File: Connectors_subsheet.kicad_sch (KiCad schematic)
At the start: 29 parts, among them J10 IMU_1, J11 USB_A, J12 Power_Connector, J3 Ultrasonic, J9 IMU_2, Q1 BSS138

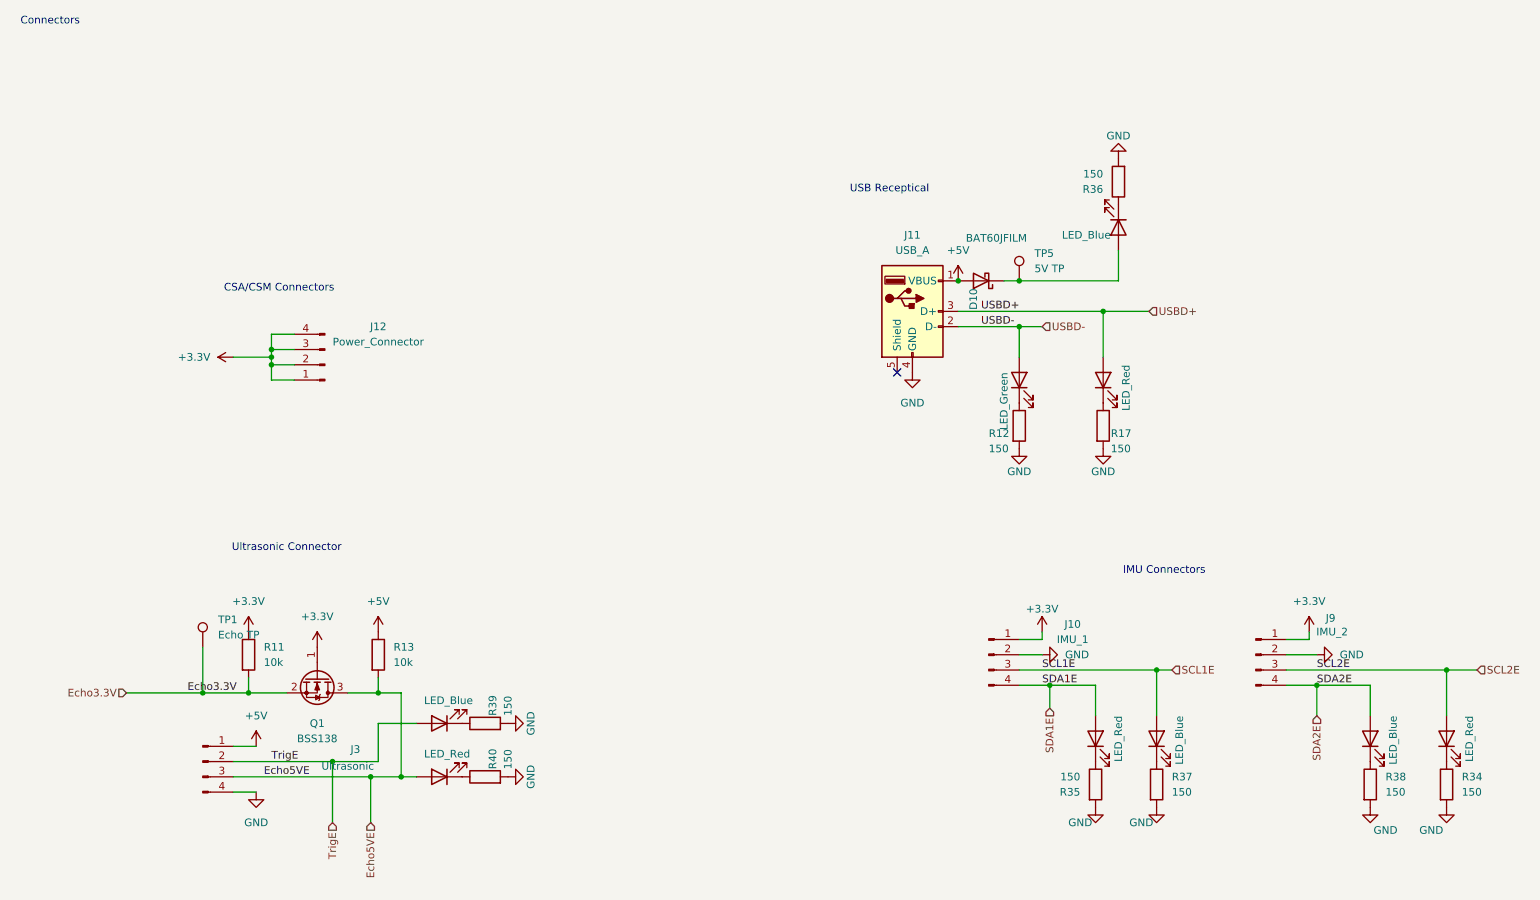
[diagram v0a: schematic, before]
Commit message: remove un-needed program header circuitry, add debug LEDs, add USB ESD, add shcotty for LM117
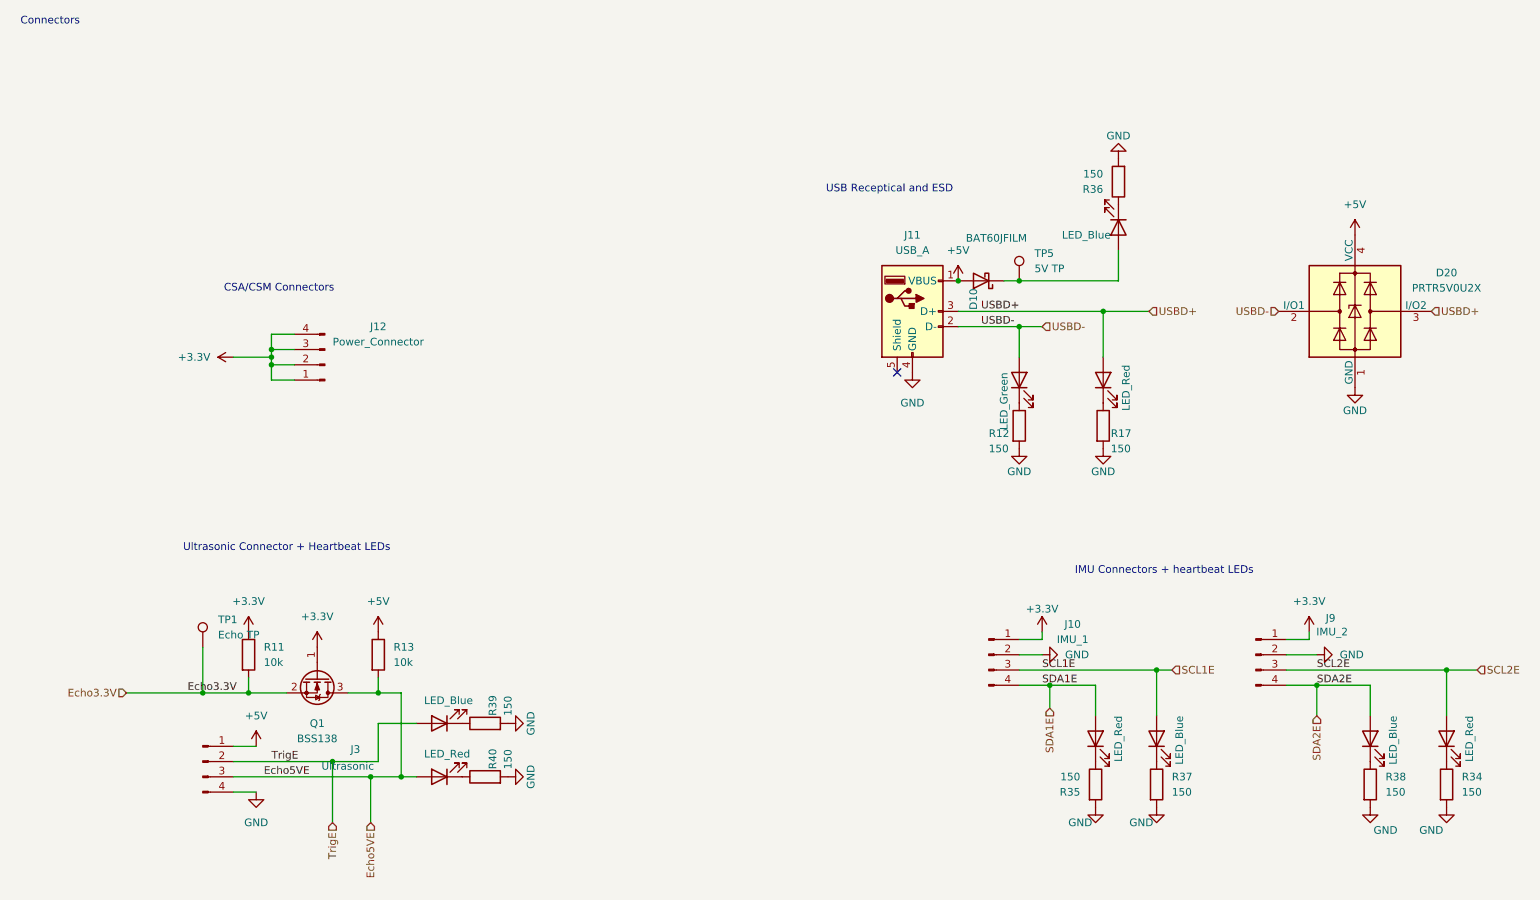
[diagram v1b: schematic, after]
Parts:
- added D20: PRTR5V0U2X, Package_TO_SOT_SMD:SOT-143, symbol Power_Protection:PRTR5V0U2X
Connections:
- net +5V: now also D20.4 (VCC)
- net GND: now also D20.1 (GND)
- net USBD+: now also D20.3 (I/O2)
- net USBD-: now also D20.2 (I/O1)
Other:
- note added: "IMU Connectors + heartbeat LEDs"
- note added: "USB Receptical and ESD"
- note added: "Ultrasonic Connector + Heartbeat LEDs"
- note removed: "IMU Connectors"
- note removed: "USB Receptical"
- note removed: "Ultrasonic Connector"
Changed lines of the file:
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@@
 		)
 	)
-	(text "Ultrasonic Connector"
+	(text "Ultrasonic Connector + Heartbeat LEDs"
 		(exclude_from_sim no)
 		(at 68.58 110.49 0)
@@
 		)
 	)
-	(text "USB Receptical\n"
+	(text "USB Receptical and ESD\n"
 		(exclude_from_sim no)
 		(at 168.91 50.8 0)
@@
 		)
 	)
-	(text "IMU Connectors\n"
+	(text "IMU Connectors + heartbeat LEDs\n"
 		(exclude_from_sim no)
 		(at 214.63 114.3 0)
@@
 		)
 	)
+	(hierarchical_label "USBD+"
+		(shape input)
+		(at 259.08 71.12 0)
+		(fields_autoplaced yes)
+		(effects
+			(font
+				(size 1.27 1.27)
+			)
+			(justify left)
+		)
+	)
 	(hierarchical_label "SDA1E"
 		(shape input)
@@
 		)
 	)
+	(hierarchical_label "USBD-"
+		(shape input)
+		(at 233.68 71.12 180)
+		(fields_autoplaced yes)
+		(effects
+			(font
+				(size 1.27 1.27)
+			)
+			(justify right)
+		)
+	)
 	(symbol
 		(lib_id "power:GND")
@@
 	)
 	(symbol
+		(lib_id "power:GND")
+		(at 246.38 83.82 0)
+		(unit 1)
+		(exclude_from_sim no)
+		(in_bom yes)
+		(on_board yes)
+		(dnp no)
+		(property "Reference" "#PWR033"
+			(at 246.38 90.17 0)
+			(effects
+				(font
+					(size 1.27 1.27)
+				)
+				(hide yes)
+			)
+		)
+		(property "Value" "GND"
+			(at 246.38 87.63 0)
+			(effects
+				(font
+					(size 1.27 1.27)
+				)
+			)
+		)
+		(property "Footprint" ""
+			(at 246.38 83.82 0)
+			(effects
+				(font
+					(size 1.27 1.27)
+				)
+				(hide yes)
+			)
+		)
+		(property "Datasheet" ""
+			(at 246.38 83.82 0)
+			(effects
+				(font
+					(size 1.27 1.27)
+				)
+				(hide yes)
+			)
+		)
+		(property "Description" "Power symbol creates a global label with name \"GND\" , ground"
+			(at 246.38 83.82 0)
+			(effects
+				(font
+					(size 1.27 1.27)
+				)
+				(hide yes)
+			)
+		)
+		(pin "1"
+		)
+		(instances
+			(project "PCB_Schematic"
+				(path "/a0c17764-e0d1-4df5-b871-1489cf266494/ca0ff4d7-ae36-445b-939c-5f82f56efbb4"
+					(reference "#PWR033")
+					(unit 1)
+				)
+			)
+		)
+	)
+	(symbol
 		(lib_id "Device:R")
 		(at 101.6 139.7 90)
@@
 	(symbol
 		(lib_id "power:+5V")
+		(at 246.38 58.42 0)
+		(unit 1)
+		(exclude_from_sim no)
+		(in_bom yes)
+		(on_board yes)
+		(dnp no)
+		(fields_autoplaced yes)
+		(property "Reference" "#PWR038"
+			(at 246.38 62.23 0)
+			(effects
+				(font
+					(size 1.27 1.27)
+				)
+				(hide yes)
+			)
+		)
+		(property "Value" "+5V"
+			(at 246.38 53.34 0)
+			(effects
+				(font
+					(size 1.27 1.27)
+				)
+			)
+		)
+		(property "Footprint" ""
+			(at 246.38 58.42 0)
+			(effects
+				(font
+					(size 1.27 1.27)
+				)
+				(hide yes)
+			)
+		)
+		(property "Datasheet" ""
+			(at 246.38 58.42 0)
+			(effects
+				(font
+					(size 1.27 1.27)
+				)
+				(hide yes)
+			)
+		)
+		(property "Description" "Power symbol creates a global label with name \"+5V\""
+			(at 246.38 58.42 0)
+			(effects
+				(font
+					(size 1.27 1.27)
+				)
+				(hide yes)
+			)
+		)
+		(pin "1"
+		)
+		(instances
+			(project "PCB_Schematic"
+				(path "/a0c17764-e0d1-4df5-b871-1489cf266494/ca0ff4d7-ae36-445b-939c-5f82f56efbb4"
+					(reference "#PWR038")
+					(unit 1)
+				)
+			)
+		)
+	)
+	(symbol
+		(lib_id "power:+5V")
 		(at 83.82 124.46 0)
 		(unit 1)
@@
 					(unit 1)
 				)
+			)
+		)
+	)
+	(symbol
+		(lib_id "Power_Protection:PRTR5V0U2X")
+		(at 246.38 71.12 0)
+		(unit 1)
+		(exclude_from_sim no)
+		(in_bom yes)
+		(on_board yes)
+		(dnp no)
+		(fields_autoplaced yes)
+		(property "Reference" "D20"
+			(at 261.62 64.6998 0)
+			(effects
+				(font
+					(size 1.27 1.27)
+				)
+			)
+		)
+		(property "Value" "PRTR5V0U2X"
+			(at 261.62 67.2398 0)
+			(effects
+				(font
+					(size 1.27 1.27)
+				)
+			)
+		)
+		(property "Footprint" "Package_TO_SOT_SMD:SOT-143"
+			(at 247.904 71.12 0)
+			(effects
+				(font
+					(size 1.27 1.27)
+				)
+				(hide yes)
+			)
+		)
+		(property "Datasheet" "https://assets.nexperia.com/documents/data-sheet/PRTR5V0U2X.pdf"
+			(at 247.904 71.12 0)
+			(effects
+				(font
+					(size 1.27 1.27)
+				)
+				(hide yes)
+			)
+		)
+		(property "Description" "Ultra low capacitance double rail-to-rail ESD protection diode, SOT-143"
+			(at 246.38 71.12 0)
+			(effects
+				(font
+					(size 1.27 1.27)
+				)
+				(hide yes)
+			)
+		)
+		(pin "1"
+		)
+		(pin "3"
+		)
+		(pin "4"
+		)
+		(pin "2"
+		)
+		(instances
+			(project ""
+				(path "/a0c17764-e0d1-4df5-b871-1489cf266494/ca0ff4d7-ae36-445b-939c-5f82f56efbb4"
+					(reference "D20")
+					(unit 1)
+				)

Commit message: starter PCB
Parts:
- renumbered D33 to D14, D34 to D15, D10 to D16, D9 to D17, D31 to D18, D13 to D19, D32 to D20, D35 to D21, D20 to D22, D36 to D23, D14 to D24, J12 to J4, J11 to J5, J10 to J6, J9 to J7, R11 to R16, R13 to R17, R39 to R18, R40 to R19, R12 to R20, R35 to R21, R17 to R22, R36 to R23, R37 to R24, R38 to R25, R34 to R26, TP1 to TP2, TP5 to TP3

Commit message: routing v1
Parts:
- added J8: SDOAG_Connector, Library:CONN_B4B-XH-A_JSTProject, symbol Connector:Conn_01x04_Pin
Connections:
- net GND: now also J8.1 (Pin_1), J8.2 (Pin_2), J8.3 (Pin_3), J8.4 (Pin_4)
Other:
- note added: "SDOAG Connectors"
- moved on the sheet: J4

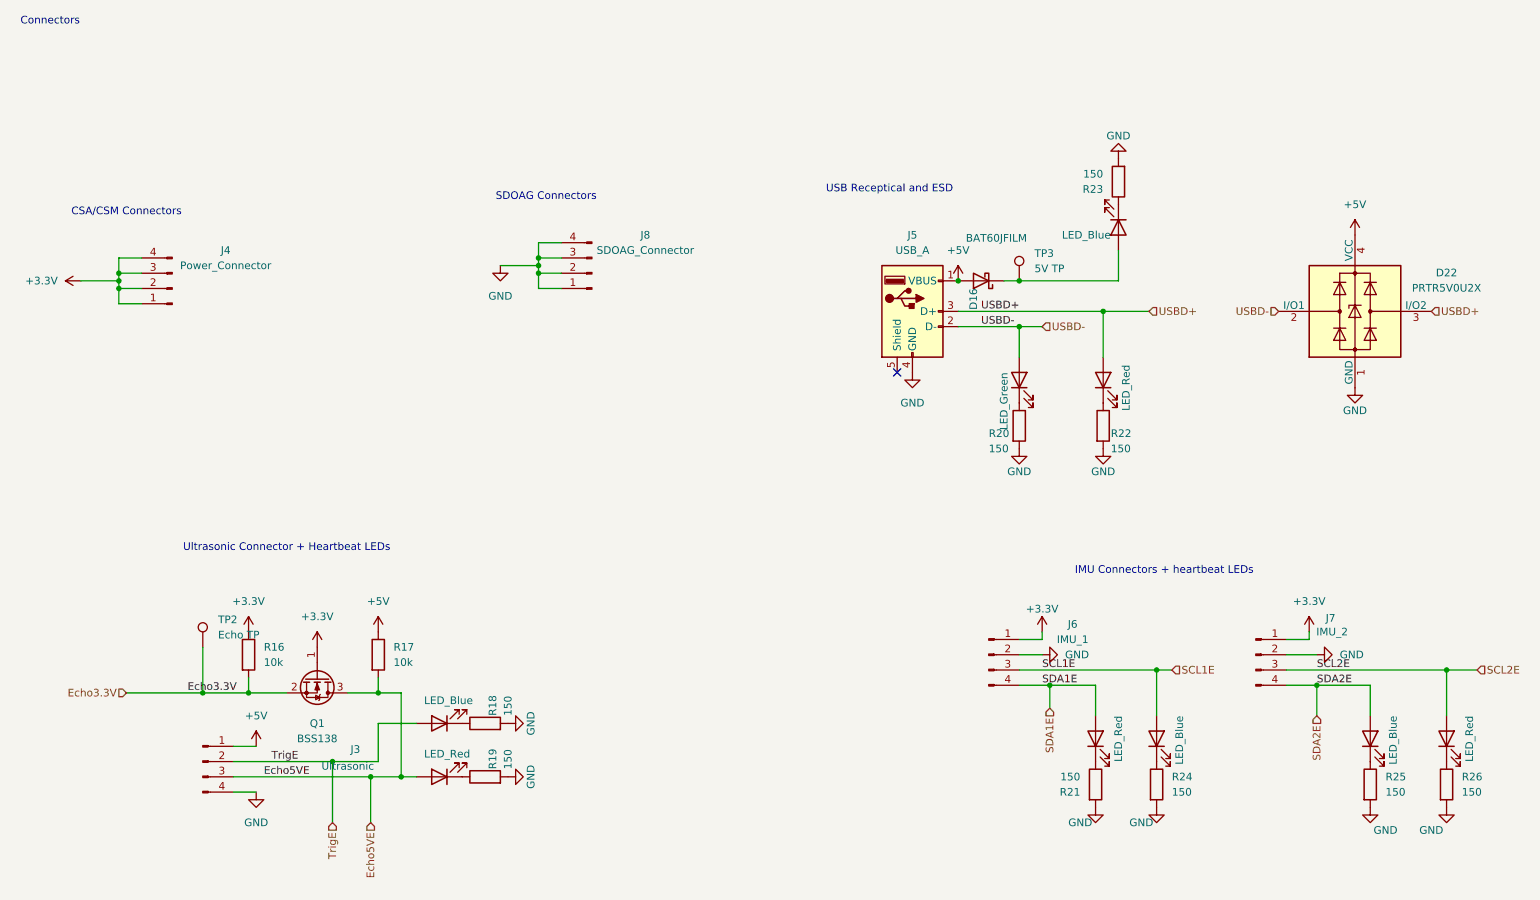
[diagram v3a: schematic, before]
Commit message: added testpoints to schematic for important sigs
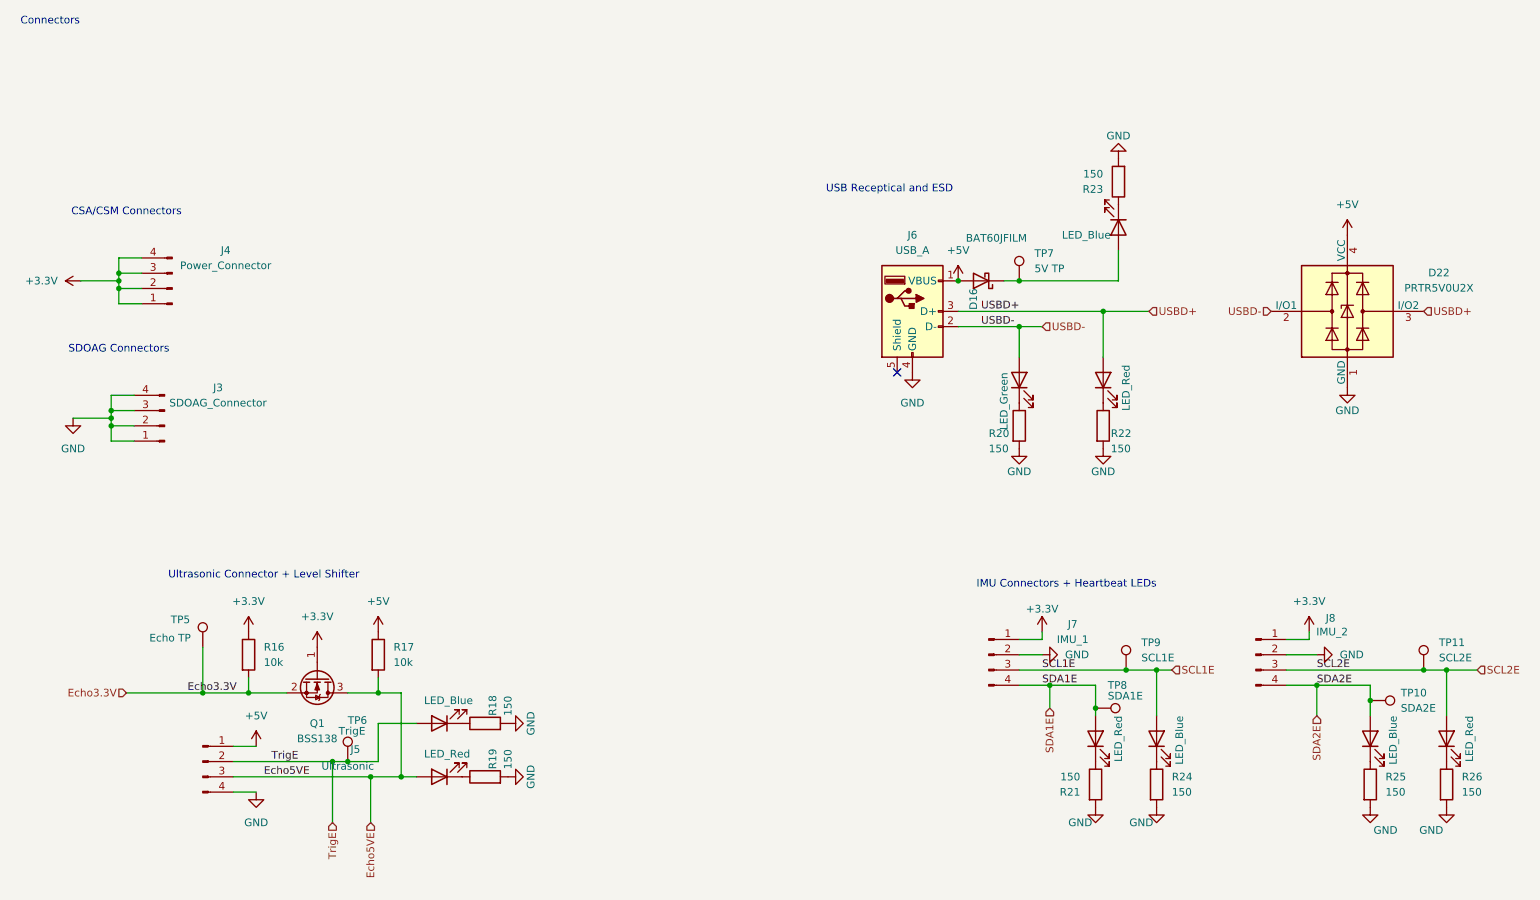
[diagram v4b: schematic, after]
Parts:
- added TP10: SDA2E, symbol Connector:TestPoint
- added TP11: SCL2E, symbol Connector:TestPoint
- added TP6: TrigE, symbol Connector:TestPoint
- added TP8: SDA1E, symbol Connector:TestPoint
- added TP9: SCL1E, symbol Connector:TestPoint
- renumbered J8 to J3, J3 to J5, J5 to J6, J6 to J7, J7 to J8, TP2 to TP5, TP3 to TP7
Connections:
- net SCL1E: now also TP9.1
- net SCL2E: now also TP11.1
- net SDA1E: now also TP8.1
- net SDA2E: now also TP10.1
- net TrigE: now also TP6.1
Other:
- note added: "IMU Connectors + Heartbeat LEDs"
- note added: "Ultrasonic Connector + Level Shifter"
- note removed: "IMU Connectors + heartbeat LEDs"
- note removed: "Ultrasonic Connector + Heartbeat LEDs"
- moved on the sheet: D22, J3

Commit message: going to set up for review
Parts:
- J6: footprint Library:Project_USB -> Connector_USB:USB_A_Receptacle_GCT_USB1046
- Q1: footprint Library:Project_BSS -> Package_TO_SOT_SMD:SOT-23-3
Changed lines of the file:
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@@
 			)
 		)
-		(property "Footprint" "Library:Project_BSS"
+		(property "Footprint" "Package_TO_SOT_SMD:SOT-23-3"
 			(at 71.755 137.16 0)
 			(effects
@@
 			)
 		)
-		(property "Footprint" "Library:Project_USB"
+		(property "Footprint" "Connector_USB:USB_A_Receptacle_GCT_USB1046"
 			(at 176.53 72.39 0)
 			(effects

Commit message: updated stuff
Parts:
- removed TP10: SDA2E, symbol Connector:TestPoint
- removed TP11: SCL2E, symbol Connector:TestPoint
- removed TP5: Echo TP, TestPoint:TestPoint_Loop_D3.50mm_Drill1.4mm_Beaded, symbol Connector:TestPoint
- removed TP6: TrigE, symbol Connector:TestPoint
- removed TP8: SDA1E, symbol Connector:TestPoint
- removed TP9: SCL1E, symbol Connector:TestPoint
- added R33, R34, R35, R36: 4.7k, Resistor_SMD:R_0805_2012Metric_Pad1.20x1.40mm_HandSolder, symbol Device:R
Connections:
- net +3.3V: now also R33.1, R34.1, R35.1, R36.1
- net SCL1E: now also R33.2
- net SCL2E: now also R36.2
- net SDA1E: now also R34.2
- net SDA2E: now also R35.2
